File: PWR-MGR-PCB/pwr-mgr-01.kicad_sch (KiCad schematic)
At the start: 26 parts, among them J3 USB_C_Receptacle_USB2.0_14P, U1 BQ24075, U5 USBLC6-2SC6, U6 TPS631011YBGR-Pin_Corrected

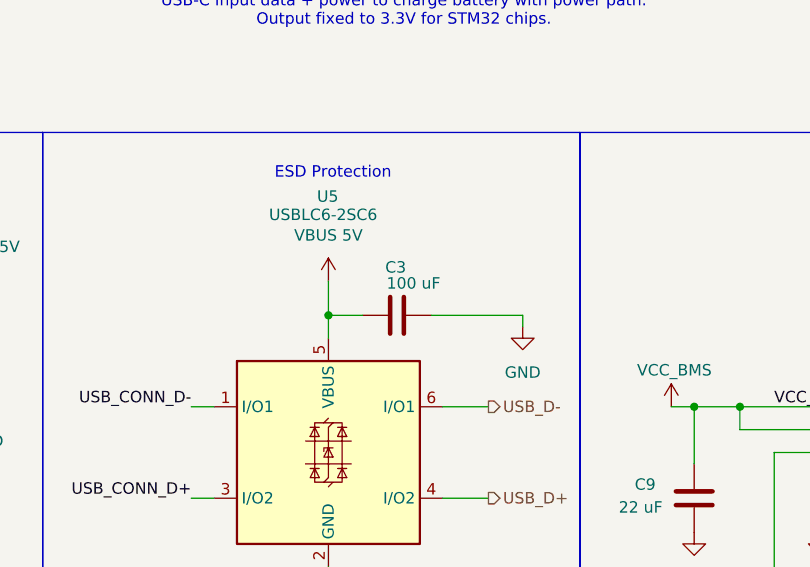
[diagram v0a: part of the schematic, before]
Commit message: fix placements + edit C3 size
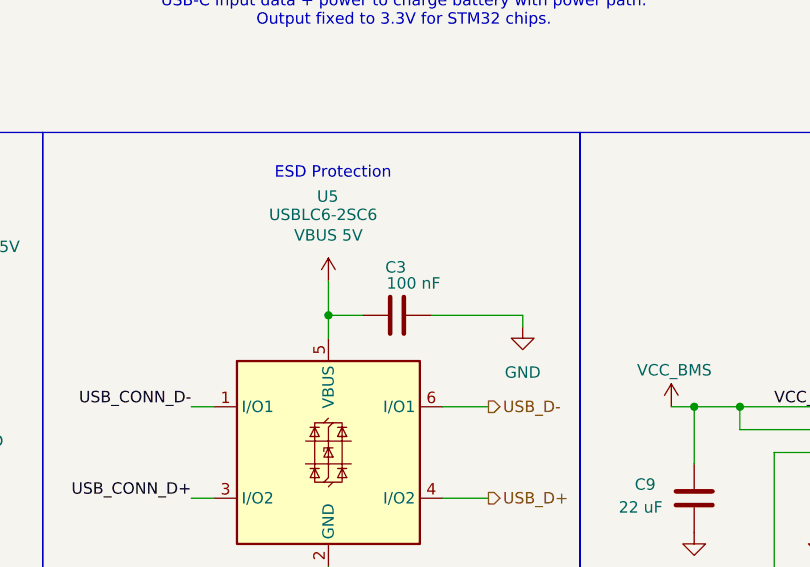
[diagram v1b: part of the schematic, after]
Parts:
- C3: value 100 uF -> 100 nF
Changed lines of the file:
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@@
 			)
 		)
-		(property "Value" "100 uF"
+		(property "Value" "100 nF"
 			(at 141.986 62.484 90)
 			(effects

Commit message: begin v2, update schematic
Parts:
- removed C10: 47 uF, Capacitor_SMD:C_0805_2012Metric, symbol Device:C
- removed C9: 22 uF, Capacitor_SMD:C_0805_2012Metric, symbol Device:C
- removed L2: DFE18SAN1R0ME0L, DFE18SAN1ROMEO Inductor:INDC1608X80N, symbol DFE18SAN1R0ME0L:DFE18SAN1R0ME0L
- removed R17: 91k, Resistor_SMD:R_0805_2012Metric, symbol Device:R
- removed R18: 511k, Resistor_SMD:R_0805_2012Metric, symbol Device:R
- removed U6: TPS631011YBGR-Pin_Corrected, DSBGA8_YBG_TEX, symbol TPS631011:TPS631011YBGR-Pin_Corrected
- added C11, C13: 22 uF, Capacitor_SMD:C_0805_2012Metric, symbol Device:C
- added C12, C14: 47 uF, Capacitor_SMD:C_0805_2012Metric, symbol Device:C
- added L1, L2: DFE252012P-1R0M=P2, DFE252012P-1R0M=P2:INDC2520X120N, symbol DFE252012P-1R0M_P2:DFE252012P-1R0M=P2
- added R19: 511k, Resistor_SMD:R_0805_2012Metric, symbol Device:R
- added R20, R22: 91k, Resistor_SMD:R_0805_2012Metric, symbol Device:R
- added R21: 820k, Resistor_SMD:R_0805_2012Metric, symbol Device:R
- added R8, R9: 100k, Resistor_SMD:R_0805_2012Metric, symbol Device:R
- added U2, U3: TPS631000DRLR, TPS631000DRLR:SOT50P160X60-8N, symbol TPS631000DRLR:TPS631000DRLR
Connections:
- net +3.3V: now also R5.2, R6.2, C12.1, R19.2, R21.2, R8.2, R9.2, U2.1 (VOUT)
- net GND: now also C11.2, C12.2, C13.2, C14.2, R20.2, R22.2, U2.6 (MODE), U2.7 (GND), U3.6 (MODE), U3.7 (GND)
- net VCC_BMS: now also C11.1, C13.1, U2.4 (VIN), U2.5 (EN), U3.4 (VIN); no longer R5.2, R6.2
- net CHG_N: now reaches D1.C
- net CHG_N: now also U1.9 (CHG), R8.1; no longer U1.7 (PGOOD)
- net PGOOD_N: now reaches D2.C
- net PGOOD_N: now also U1.7 (PGOOD), R9.1; no longer U1.9 (CHG)
- new net: R19.1, R20.1, U2.8 (FB)
- new net: L2.1, U2.2 (LX2)
- new net: L2.2, U2.3 (LX1)
- new net: L1.1, U3.2 (LX2)
- new net: L1.2, U3.3 (LX1)
- new net: R21.1, R22.1, U3.8 (FB)
- new net +5V: C14.1, U3.1 (VOUT)
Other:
- note added: "Buck Boost Converter 3.3V Rail"
- note added: "Buck Boost Converter 5V Rail"
- note removed: "Buck Boost Converter"
- moved on the sheet: C3, C4, C5, C6, D1, NT1, R1, R2, R3, R4, R7, U1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

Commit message: complete schematic
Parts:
- removed D3: SS34, Diode_SMD:D_SMA, symbol Diode:SS34
- added C7: 100n, Capacitor_SMD:C_0805_2012Metric, symbol Device:C
- added D3: SMF12A, Diode_SMD:D_SMF, symbol Diode:SMF12A
- added R10: 100k, Resistor_SMD:R_0805_2012Metric, symbol Device:R
- added R11, R15: 1M, Resistor_SMD:R_0805_2012Metric, symbol Device:R
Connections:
- net +3.3V: now also C3.1, U5.5 (VBUS); no longer R21.2
- net +5V: now also R21.2
- net BAT+: now also R11.1
- net GND: now also C7.1, D3.2 (A2), R10.1, R15.2
- net VBUS 5V: now also J3.A4 (VBUS), J3.A9 (VBUS), J3.B4 (VBUS), J3.B9 (VBUS), D3.1 (A1); no longer C3.1, U5.5 (VBUS)
- net 5V_ENABLE: now reaches U3.5 (EN)
- net 5V_ENABLE: now also R10.2
- new net VBAT_SENSE: C7.2, R11.2, R15.1
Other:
- note removed: "Two 5.1k resistors on USB-C CC1 and CC2 will draw 0.5 to 0.9A @ 5V"
- moved on the sheet: C13, R9

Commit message: fix footprint issues, route regulators
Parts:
- removed NT1: NetTie_2, symbol Device:NetTie_2
- L1, L2: footprint DFE252012P-1R0M=P2:INDC2520X120N -> DFE252012P_1R0M_P2:INDC2520X120N
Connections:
- net VCC_BMS: now also U1.11 (OUT)
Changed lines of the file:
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@@
 	(wire
 		(pts
-			(xy 102.87 146.05) (xy 102.87 149.86)
-		)
-		(stroke
-			(width 0)
-			(type default)
-		)
-	)
-	(wire
-		(pts
 			(xy 57.15 130.81) (xy 55.88 130.81)
 		)
@@
 	(wire
 		(pts
-			(xy 105.41 143.51) (xy 105.41 144.78)
+			(xy 105.41 143.51) (xy 105.41 146.05)
 		)
 		(stroke
@@
 	(wire
 		(pts
-			(xy 102.87 149.86) (xy 105.41 149.86)
-		)
-		(stroke
-			(width 0)
-			(type default)
-		)
-	)
-	(wire
-		(pts
 			(xy 254 132.08) (xy 254 133.35)
 		)
@@
 	(wire
 		(pts
+			(xy 102.87 146.05) (xy 105.41 146.05)
+		)
+		(stroke
+			(width 0)
+			(type default)
+		)
+	)
+	(wire
+		(pts
 			(xy 223.52 92.71) (xy 220.98 92.71)
 		)
@@
 			)
 		)
-		(property "Footprint" "DFE252012P-1R0M=P2:INDC2520X120N"
+		(property "Footprint" "DFE252012P_1R0M_P2:INDC2520X120N"
 			(at 234.95 140.97 0)
 			(hide yes)
@@
 			)
 		)
-		(property "Footprint" "DFE252012P-1R0M=P2:INDC2520X120N"
+		(property "Footprint" "DFE252012P_1R0M_P2:INDC2520X120N"
 			(at 232.41 80.01 0)
 			(hide yes)
@@
 					(unit 1)
 				)
-			)
-		)
-	)
-	(symbol
-		(lib_id "Device:NetTie_2")
-		(at 105.41 147.32 90)
-		(unit 1)
-		(body_style 1)
-		(exclude_from_sim no)
-		(in_bom no)
-		(on_board yes)
-		(in_pos_files yes)
-		(dnp no)
-		(property "Reference" "NT1"
-			(at 103.632 141.986 90)
-			(show_name no)
-			(do_not_autoplace no)
-			(effects
-				(font
-					(size 1.27 1.27)
-				)
-				(justify right)
-			)
-		)
-		(property "Value" "NetTie_2"
-			(at 107.442 141.986 90)
-			(show_name no)
-			(do_not_autoplace no)
-			(effects
-				(font
-					(size 1.27 1.27)
-				)
-				(justify right)
-			)
-		)
-		(property "Footprint" ""
-			(at 105.41 147.32 0)
-			(hide yes)
-			(show_name no)
-			(do_not_autoplace no)
-			(effects
-				(font
-					(size 1.27 1.27)
-				)
-			)
-		)
-		(property "Datasheet" ""
-			(at 105.41 147.32 0)
-			(hide yes)
-			(show_name no)
-			(do_not_autoplace no)
-			(effects
-				(font
-					(size 1.27 1.27)
-				)
-			)
-		)
-		(property "Description" "Net tie, 2 pins"
-			(at 105.41 147.32 0)
-			(hide yes)
-			(show_name no)
-			(do_not_autoplace no)
-			(effects
-				(font
-					(size 1.27 1.27)
-				)
-			)
-		)
-		(pin "2"
-		)
-		(pin "1"
-		)
-		(instances
-			(project "PWR-MGR-PCB"
-				(path "/16b2e4e2-6399-42b6-a8e6-a11780888710/aa25d2a4-7317-40e7-833e-e05b81834ee4"
-					(reference "NT1")
-					(unit 1)
-				)

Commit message: route signals
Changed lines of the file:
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@@
 		(property "Reference" "R6"
 			(at 60.96 128.524 90)
-			(hide yes)
 			(show_name no)
 			(do_not_autoplace no)

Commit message: finish routing
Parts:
- added R4B1: 10k, Resistor_SMD:R_0805_2012Metric_Pad1.20x1.40mm_HandSolder, symbol Device:R
- R4: footprint Resistor_SMD:R_0805_2012Metric -> Resistor_SMD:R_0805_2012Metric_Pad1.20x1.40mm_HandSolder
- renumbered C7 to C1, C5 to C2, C4 to C3, C6 to C4, C3 to C5, C13 to C6, C11 to C7, C12 to C8, C14 to C9, D2 to D1, D3 to D2, D1 to D3, J3 to J23, L2 to L1, L1 to L2, R15 to R1, R2 to R10, R8 to R11, R7 to R12, R5 to R13, R10 to R14, R19 to R15, R20 to R16, R21 to R17, R22 to R18, R11 to R2, R6 to R3, R9 to R5, R12 to R6, R3 to R7, R1 to R8, R13 to R9, U5 to U2, U2 to U3, U3 to U4
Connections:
- net GND: now also R4B1.1
- net at R4.2, U1.1 (TS): now also R4B1.2
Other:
- note added: "R4B1 is an alternate location for a thermistor. Do not populate BOTH R4 and R4B1 at the same time."
